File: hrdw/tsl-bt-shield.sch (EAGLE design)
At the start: 13 parts, among them U1 HC_05

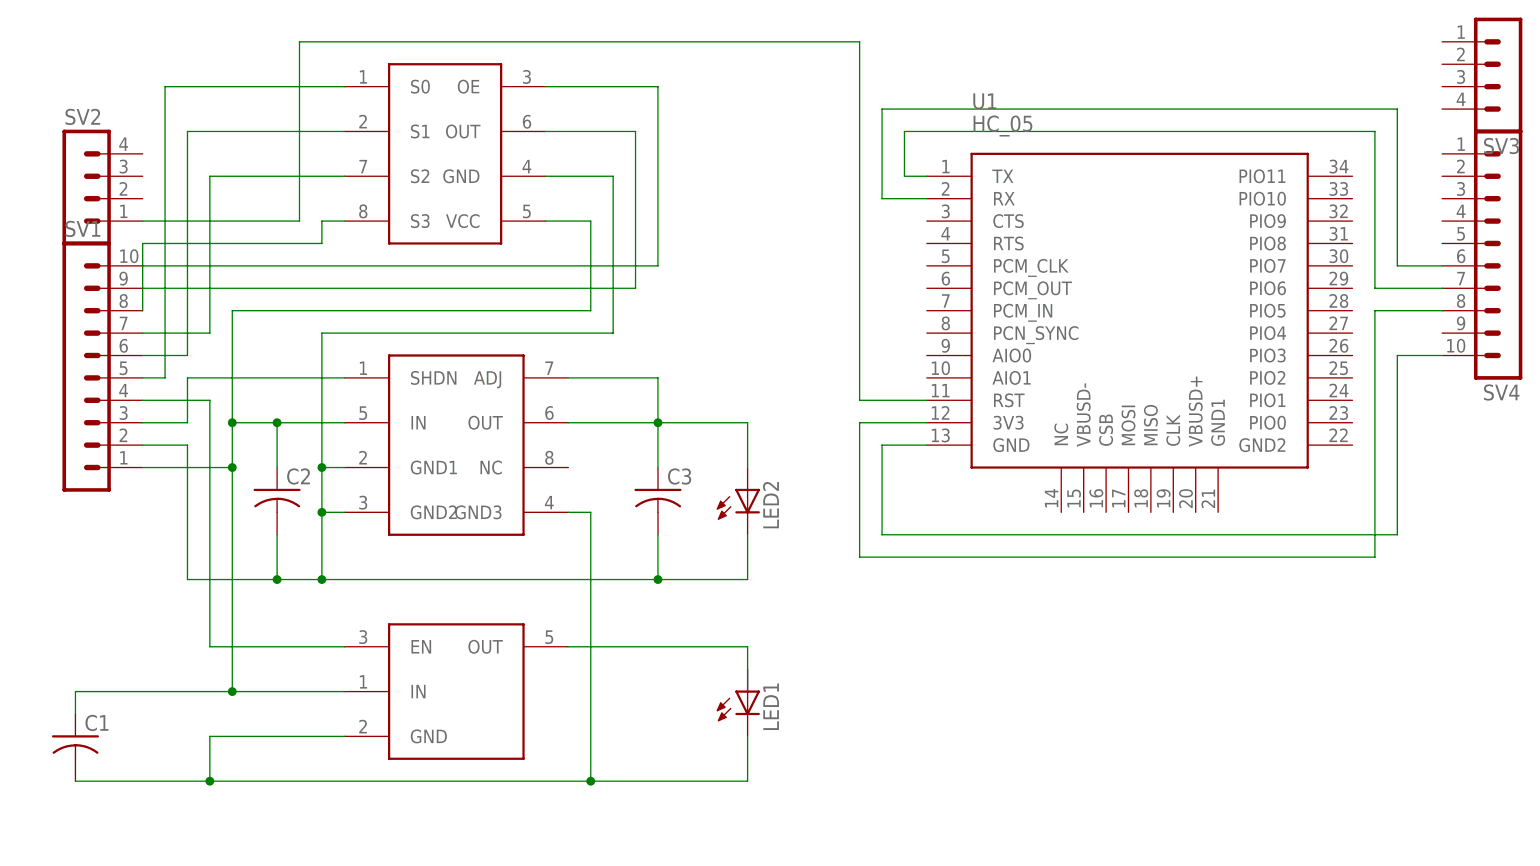
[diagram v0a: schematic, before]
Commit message: [master] TSL board design finalized
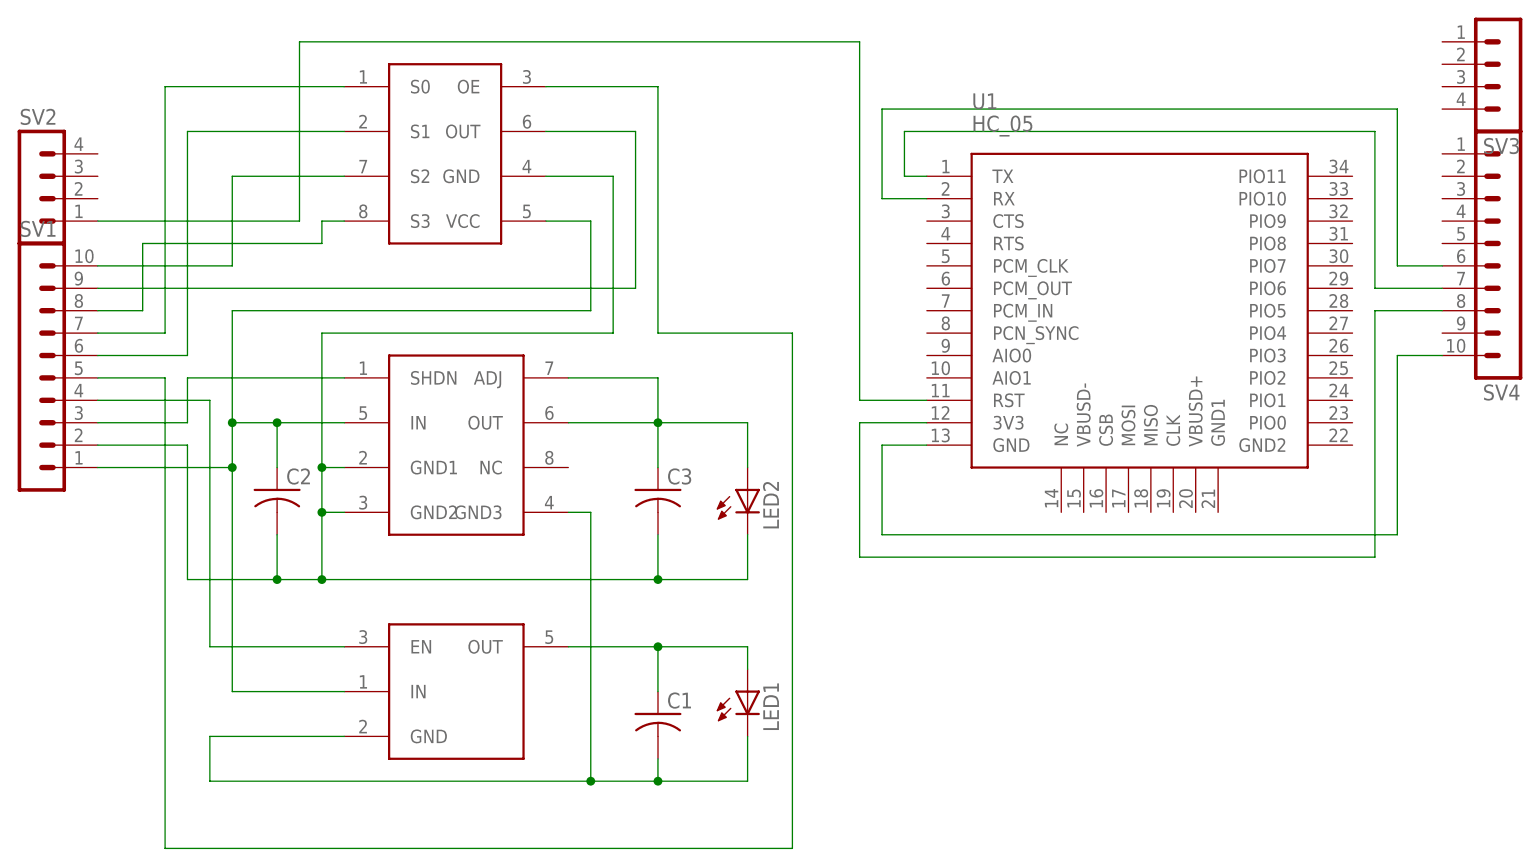
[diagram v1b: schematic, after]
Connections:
- net N$1: no longer C1.1
- net N$11: now also SV1.10; no longer SV1.7
- net N$3: now also C1.1, LED1.A
- net N$8: now also SV1.5; no longer SV1.10
- net N$9: now also SV1.7; no longer SV1.5
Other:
- moved on the sheet: C1, SV1, SV2
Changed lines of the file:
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@@
 <part name="SV4" library="con-lstb" deviceset="MA10-1" device=""/>
 <part name="LED1" library="led" deviceset="LED" device=""/>
-<part name="C1" library="rcl" deviceset="C-US" device="C1206K"/>
 <part name="C2" library="rcl" deviceset="C-US" device="C1206K"/>
 <part name="C3" library="rcl" deviceset="C-US" device="C1206K"/>
 <part name="LED2" library="led" deviceset="LED" device=""/>
 <part name="U$3" library="Sleepwalker" deviceset="TSL230" device=""/>
+<part name="C1" library="rcl" deviceset="C-US" device="C1206K"/>
 </parts>
 <sheets>
@@
 <instance part="U$1" gate="G$1" x="86.36" y="48.26"/>
 <instance part="U$2" gate="G$1" x="76.2" y="17.78"/>
-<instance part="SV1" gate="1" x="15.24" y="60.96"/>
-<instance part="SV2" gate="1" x="15.24" y="83.82"/>
+<instance part="SV1" gate="1" x="10.16" y="60.96"/>
+<instance part="SV2" gate="1" x="10.16" y="83.82"/>
 <instance part="SV3" gate="1" x="177.8" y="93.98" rot="R180"/>
 <instance part="SV4" gate="1" x="177.8" y="76.2" rot="R180"/>
 <instance part="LED1" gate="G$1" x="91.44" y="25.4"/>
-<instance part="C1" gate="G$1" x="15.24" y="20.32"/>
 <instance part="C2" gate="G$1" x="38.1" y="48.26"/>
 <instance part="C3" gate="G$1" x="81.28" y="48.26"/>
 <instance part="LED2" gate="G$1" x="91.44" y="48.26"/>
 <instance part="U$3" gate="G$1" x="53.34" y="78.74"/>
+<instance part="C1" gate="G$1" x="81.28" y="22.86"/>
 </instances>
 <busses>
@@
 <segment>
 <pinref part="SV1" gate="1" pin="1"/>
-<wire x1="22.86" y1="50.8" x2="33.02" y2="50.8" width="0.1524" layer="91"/>
+<wire x1="17.78" y1="50.8" x2="33.02" y2="50.8" width="0.1524" layer="91"/>
 <wire x1="33.02" y1="50.8" x2="33.02" y2="55.88" width="0.1524" layer="91"/>
 <wire x1="33.02" y1="55.88" x2="38.1" y2="55.88" width="0.1524" layer="91"/>
@@
 <wire x1="38.1" y1="55.88" x2="38.1" y2="50.8" width="0.1524" layer="91"/>
 <junction x="38.1" y="55.88"/>
-<wire x1="33.02" y1="25.4" x2="15.24" y2="25.4" width="0.1524" layer="91"/>
-<pinref part="C1" gate="G$1" pin="1"/>
-<wire x1="15.24" y1="25.4" x2="15.24" y2="22.86" width="0.1524" layer="91"/>
-<junction x="33.02" y="25.4"/>
 <pinref part="U$3" gate="G$1" pin="VCC"/>
 </segment>
@@
 <pinref part="LED1" gate="G$1" pin="C"/>
 <wire x1="91.44" y1="20.32" x2="91.44" y2="15.24" width="0.1524" layer="91"/>
-<wire x1="91.44" y1="15.24" x2="73.66" y2="15.24" width="0.1524" layer="91"/>
+<wire x1="91.44" y1="15.24" x2="81.28" y2="15.24" width="0.1524" layer="91"/>
 <pinref part="LED2" gate="G$1" pin="C"/>
+<wire x1="81.28" y1="15.24" x2="73.66" y2="15.24" width="0.1524" layer="91"/>
 <wire x1="91.44" y1="43.18" x2="91.44" y2="38.1" width="0.1524" layer="91"/>
 <wire x1="91.44" y1="38.1" x2="81.28" y2="38.1" width="0.1524" layer="91"/>
@@
 <pinref part="SV1" gate="1" pin="2"/>
 <wire x1="81.28" y1="38.1" x2="73.66" y2="38.1" width="0.1524" layer="91"/>
-<wire x1="22.86" y1="53.34" x2="27.94" y2="53.34" width="0.1524" layer="91"/>
+<wire x1="17.78" y1="53.34" x2="27.94" y2="53.34" width="0.1524" layer="91"/>
 <wire x1="27.94" y1="53.34" x2="27.94" y2="38.1" width="0.1524" layer="91"/>
 <wire x1="27.94" y1="38.1" x2="38.1" y2="38.1" width="0.1524" layer="91"/>
@@
 <wire x1="38.1" y1="43.18" x2="38.1" y2="38.1" width="0.1524" layer="91"/>
 <junction x="38.1" y="38.1"/>
+<pinref part="U$3" gate="G$1" pin="GND"/>
+<junction x="81.28" y="15.24"/>
 <pinref part="C1" gate="G$1" pin="2"/>
-<wire x1="15.24" y1="15.24" x2="30.48" y2="15.24" width="0.1524" layer="91"/>
-<junction x="30.48" y="15.24"/>
-<pinref part="U$3" gate="G$1" pin="GND"/>
+<wire x1="81.28" y1="17.78" x2="81.28" y2="15.24" width="0.1524" layer="91"/>
 </segment>
 </net>
@@
 <segment>
 <pinref part="U$2" gate="G$1" pin="OUT"/>
-<wire x1="71.12" y1="30.48" x2="91.44" y2="30.48" width="0.1524" layer="91"/>
-<wire x1="91.44" y1="30.48" x2="91.44" y2="25.4" width="0.1524" layer="91"/>
+<wire x1="71.12" y1="30.48" x2="81.28" y2="30.48" width="0.1524" layer="91"/>
+<wire x1="91.44" y1="30.48" x2="91.44" y2="27.94" width="0.1524" layer="91"/>
+<pinref part="LED1" gate="G$1" pin="A"/>
+<wire x1="91.44" y1="30.48" x2="81.28" y2="30.48" width="0.1524" layer="91"/>
+<wire x1="81.28" y1="30.48" x2="81.28" y2="25.4" width="0.1524" layer="91"/>
+<pinref part="C1" gate="G$1" pin="1"/>
+<junction x="81.28" y="30.48"/>
 </segment>
 </net>
@@
 <wire x1="45.72" y1="30.48" x2="30.48" y2="30.48" width="0.1524" layer="91"/>
 <wire x1="30.48" y1="30.48" x2="30.48" y2="58.42" width="0.1524" layer="91"/>
-<wire x1="30.48" y1="58.42" x2="22.86" y2="58.42" width="0.1524" layer="91"/>
+<wire x1="30.48" y1="58.42" x2="17.78" y2="58.42" width="0.1524" layer="91"/>
 <pinref part="SV1" gate="1" pin="4"/>
 </segment>
@@
 <segment>
 <pinref part="SV1" gate="1" pin="3"/>
-<wire x1="22.86" y1="55.88" x2="27.94" y2="55.88" width="0.1524" layer="91"/>
+<wire x1="17.78" y1="55.88" x2="27.94" y2="55.88" width="0.1524" layer="91"/>
 <wire x1="27.94" y1="55.88" x2="27.94" y2="60.96" width="0.1524" layer="91"/>
 <wire x1="27.94" y1="60.96" x2="45.72" y2="60.96" width="0.1524" layer="91"/>
@@
 <segment>
 <pinref part="SV1" gate="1" pin="9"/>
-<wire x1="22.86" y1="71.12" x2="78.74" y2="71.12" width="0.1524" layer="91"/>
+<wire x1="17.78" y1="71.12" x2="78.74" y2="71.12" width="0.1524" layer="91"/>
 <wire x1="78.74" y1="71.12" x2="78.74" y2="88.9" width="0.1524" layer="91"/>
 <wire x1="78.74" y1="88.9" x2="68.58" y2="88.9" width="0.1524" layer="91"/>
@@
 <segment>
 <wire x1="68.58" y1="93.98" x2="81.28" y2="93.98" width="0.1524" layer="91"/>
-<wire x1="81.28" y1="93.98" x2="81.28" y2="73.66" width="0.1524" layer="91"/>
-<pinref part="SV1" gate="1" pin="10"/>
-<wire x1="81.28" y1="73.66" x2="22.86" y2="73.66" width="0.1524" layer="91"/>
+<wire x1="81.28" y1="93.98" x2="81.28" y2="66.04" width="0.1524" layer="91"/>
 <pinref part="U$3" gate="G$1" pin="OE"/>
-</segment>
-</net>
-<net name="N$9" class="0">
-<segment>
+<wire x1="81.28" y1="66.04" x2="96.52" y2="66.04" width="0.1524" layer="91"/>
+<wire x1="96.52" y1="66.04" x2="96.52" y2="7.62" width="0.1524" layer="91"/>
 <pinref part="SV1" gate="1" pin="5"/>
-<wire x1="22.86" y1="60.96" x2="25.4" y2="60.96" width="0.1524" layer="91"/>
-<wire x1="25.4" y1="60.96" x2="25.4" y2="93.98" width="0.1524" layer="91"/>
-<wire x1="25.4" y1="93.98" x2="45.72" y2="93.98" width="0.1524" layer="91"/>
-<pinref part="U$3" gate="G$1" pin="S0"/>
+<wire x1="17.78" y1="60.96" x2="25.4" y2="60.96" width="0.1524" layer="91"/>
+<wire x1="96.52" y1="7.62" x2="25.4" y2="7.62" width="0.1524" layer="91"/>
+<wire x1="25.4" y1="7.62" x2="25.4" y2="60.96" width="0.1524" layer="91"/>
 </segment>
 </net>
@@
 <segment>
 <pinref part="SV1" gate="1" pin="6"/>
-<wire x1="22.86" y1="63.5" x2="27.94" y2="63.5" width="0.1524" layer="91"/>
+<wire x1="17.78" y1="63.5" x2="27.94" y2="63.5" width="0.1524" layer="91"/>
 <wire x1="27.94" y1="63.5" x2="27.94" y2="88.9" width="0.1524" layer="91"/>
 <wire x1="27.94" y1="88.9" x2="45.72" y2="88.9" width="0.1524" layer="91"/>
@@
 </segment>
 </net>
-<net name="N$11" class="0">
-<segment>
-<pinref part="SV1" gate="1" pin="7"/>
-<wire x1="22.86" y1="66.04" x2="30.48" y2="66.04" width="0.1524" layer="91"/>
-<wire x1="30.48" y1="66.04" x2="30.48" y2="83.82" width="0.1524" layer="91"/>
-<wire x1="30.48" y1="83.82" x2="45.72" y2="83.82" width="0.1524" layer="91"/>
-<pinref part="U$3" gate="G$1" pin="S2"/>
-</segment>
-</net>
 <net name="N$12" class="0">
 <segment>
-<pinref part="SV1" gate="1" pin="8"/>
-<wire x1="22.86" y1="68.58" x2="22.86" y2="76.2" width="0.1524" layer="91"/>
 <wire x1="22.86" y1="76.2" x2="43.18" y2="76.2" width="0.1524" layer="91"/>
 <wire x1="43.18" y1="76.2" x2="43.18" y2="78.74" width="0.1524" layer="91"/>
 <wire x1="43.18" y1="78.74" x2="45.72" y2="78.74" width="0.1524" layer="91"/>
 <pinref part="U$3" gate="G$1" pin="S3"/>
+<pinref part="SV1" gate="1" pin="8"/>
+<wire x1="17.78" y1="68.58" x2="22.86" y2="68.58" width="0.1524" layer="91"/>
+<wire x1="22.86" y1="68.58" x2="22.86" y2="76.2" width="0.1524" layer="91"/>
 </segment>
 </net>
@@
 <segment>
 <pinref part="SV2" gate="1" pin="1"/>
-<wire x1="22.86" y1="78.74" x2="40.64" y2="78.74" width="0.1524" layer="91"/>
+<wire x1="17.78" y1="78.74" x2="40.64" y2="78.74" width="0.1524" layer="91"/>
 <wire x1="40.64" y1="78.74" x2="40.64" y2="99.06" width="0.1524" layer="91"/>
 <wire x1="40.64" y1="99.06" x2="104.14" y2="99.06" width="0.1524" layer="91"/>
@@
 </segment>
 </net>
+<net name="N$9" class="0">
+<segment>
+<pinref part="U$3" gate="G$1" pin="S0"/>
+<wire x1="45.72" y1="93.98" x2="25.4" y2="93.98" width="0.1524" layer="91"/>
+<wire x1="25.4" y1="93.98" x2="25.4" y2="66.04" width="0.1524" layer="91"/>
+<wire x1="25.4" y1="66.04" x2="17.78" y2="66.04" width="0.1524" layer="91"/>
+<pinref part="SV1" gate="1" pin="7"/>
+</segment>
+</net>
+<net name="N$11" class="0">
+<segment>
+<pinref part="U$3" gate="G$1" pin="S2"/>
+<wire x1="45.72" y1="83.82" x2="33.02" y2="83.82" width="0.1524" layer="91"/>
+<wire x1="33.02" y1="83.82" x2="33.02" y2="73.66" width="0.1524" layer="91"/>
+<pinref part="SV1" gate="1" pin="10"/>
+<wire x1="33.02" y1="73.66" x2="17.78" y2="73.66" width="0.1524" layer="91"/>
+</segment>
+</net>
